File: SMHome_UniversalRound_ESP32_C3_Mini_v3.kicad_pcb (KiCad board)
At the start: 2 copper layers, 48 x 45.6 mm, 58 parts, among them J1 K128_P3, J2 K128_P4, J3 Disp, J4 220V, J5 K128_P3, J6 JST SH, J7 USB_C_Receptacle_PowerOnly_6P, J8 Bat, Q1 IRLML6402, U1 ESP32 C3 Pro Mini, U2 BP2525F, U3 LP5907MFX-3.3, U4 MCP73831/2

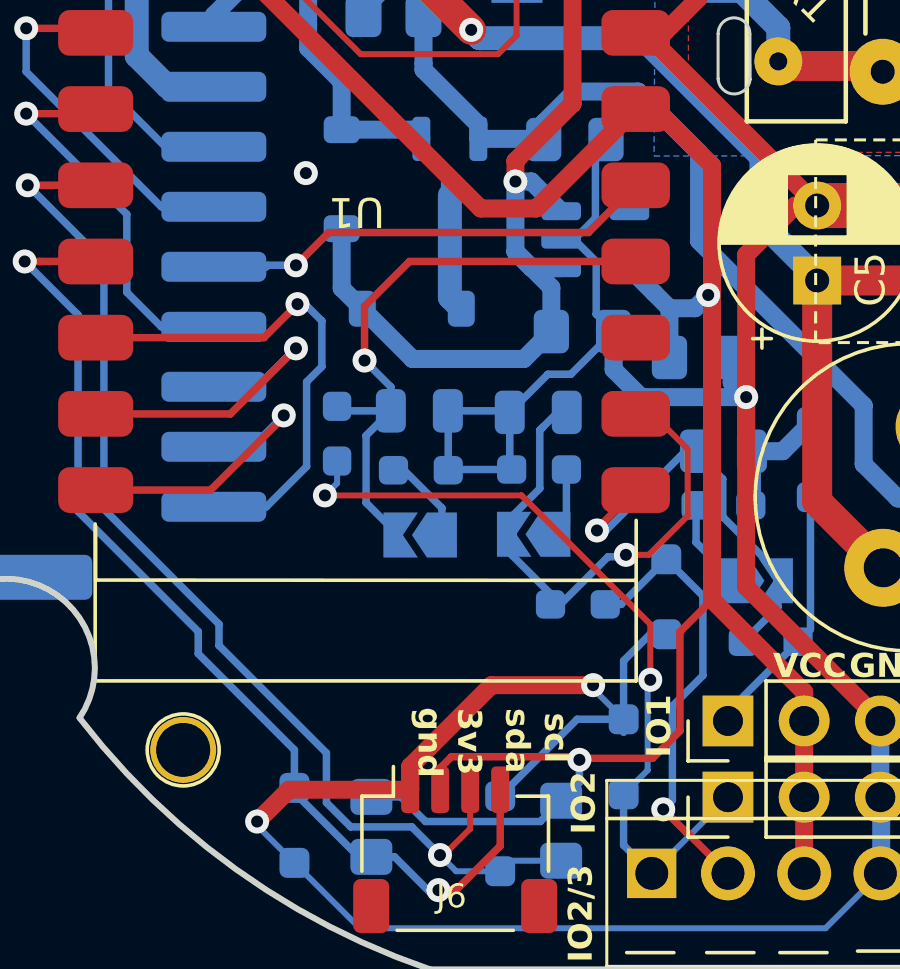
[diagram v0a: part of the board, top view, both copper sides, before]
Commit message: Migrate to KiKad 9
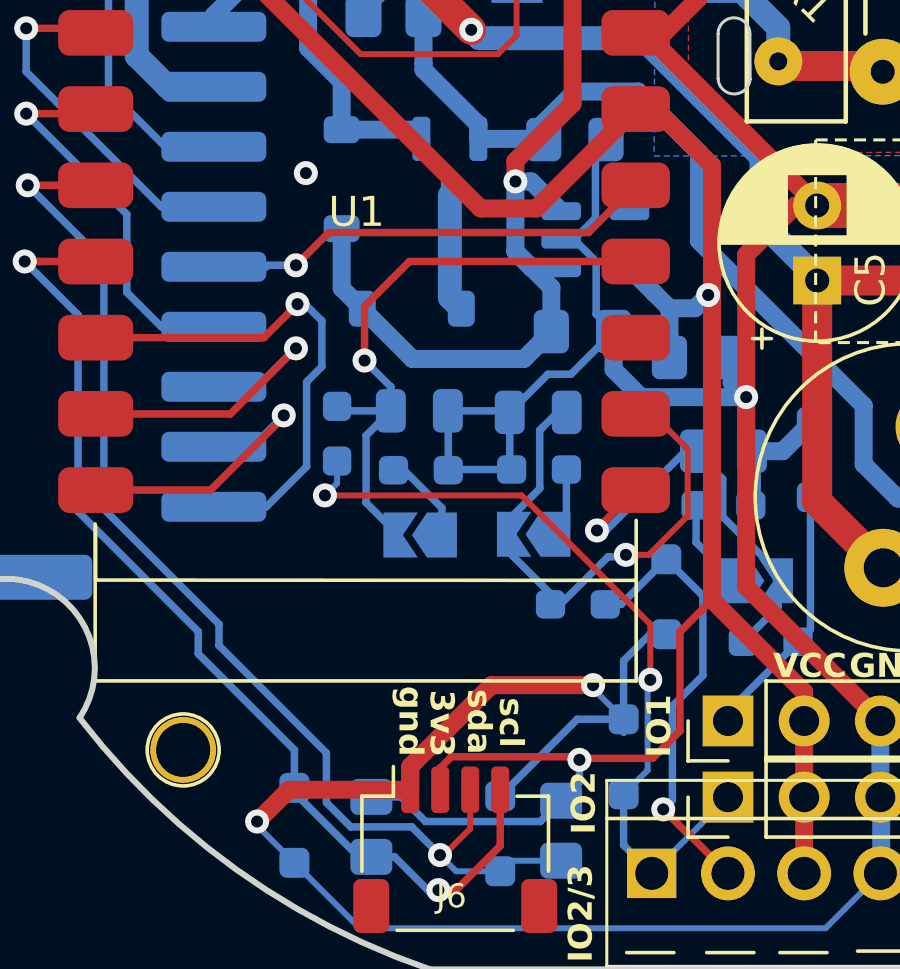
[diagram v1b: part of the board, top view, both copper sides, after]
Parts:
- J3: value Disp -> S8B-PH-SM4-TB
- J4: value 220V -> 220V input Screw connector pitch 5мм
- R5: value 10 -> 10R
